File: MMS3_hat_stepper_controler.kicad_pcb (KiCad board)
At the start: 4 copper layers, 90 x 50 mm, 77 parts, among them J1 Chainbus in, J10 Conn_01x02, J11 Conn_01x02, J12 Conn_01x02, J2 Chainbus Out, J3 Conn_01x04_Pin, J4 AMASS XT60 Male, J5 AMASS XT60 Female, J6 Encoder connector, J7 Motor connector, J8 Conn_01x03_Pin, J9 Conn_01x02, U1 SN74CB3Q3384APW, U2 M24C64, U3 TMC5130A-TA, U4 AMS1117, U5 LM2596HVS-ADJRG

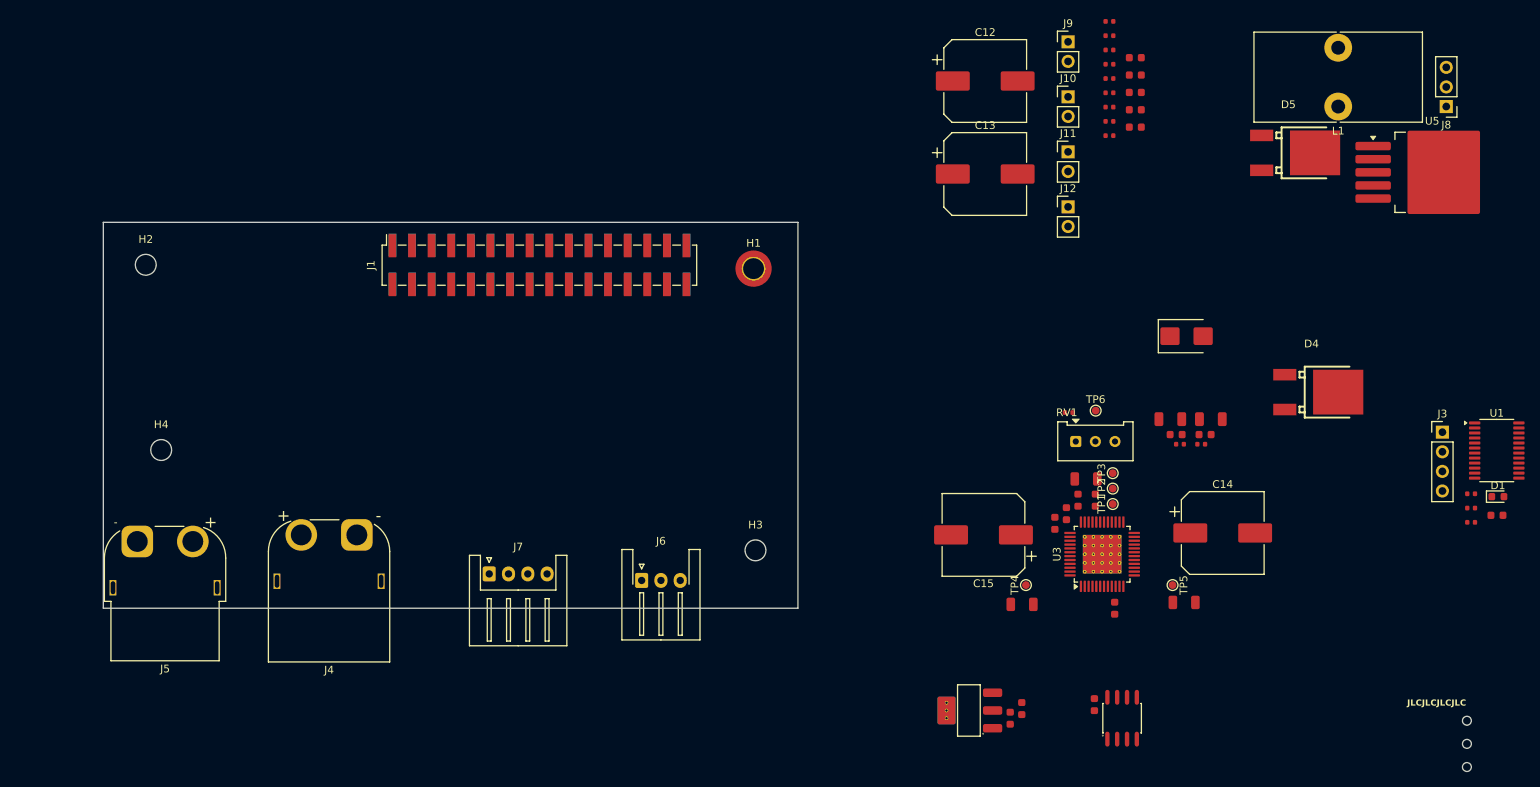
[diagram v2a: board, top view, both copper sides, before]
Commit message: added PCB from mechanical template
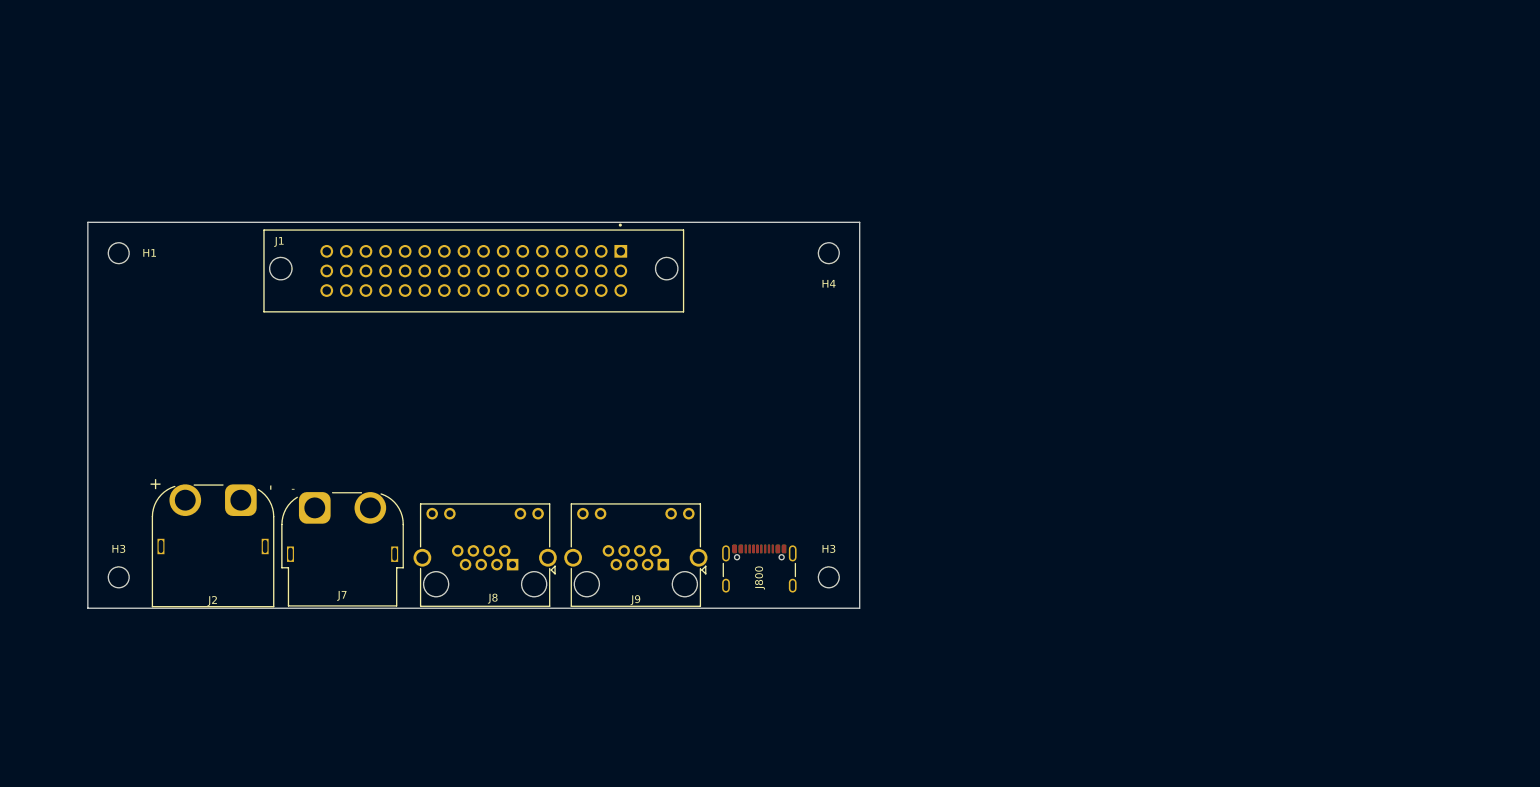
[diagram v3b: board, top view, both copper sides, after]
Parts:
- removed C1, C18, C19, C2, C21, C22, C3, C7, C8, C9: 100nF, PCM_JLCPCB:C_0603
- removed C10, C11: 4.7uF, PCM_JLCPCB:C_1206
- removed C12, C13, C14, C15: 100u, Capacitor_SMD:CP_Elec_10x12.5
- removed C16, C17: 10uF, PCM_JLCPCB:C_0603
- removed C20: 3.3nF, PCM_JLCPCB:C_0603
- removed C4: 4.7uF, PCM_JLCPCB:C_0603
- removed C5: 22nF, PCM_JLCPCB:C_0603
- removed C6: 470nF, PCM_JLCPCB:C_0603
- removed D1: LED, LED_SMD:LED_0603_1608Metric
- removed D3: SMBJ43CA, PCM_JLCPCB:D_SMB
- removed D4, D5: MBRD10100CTTR, SMC_MBRD10100CTTR:TO-252-3_L6.5-W5.8-P4.58-TL
- removed H2: M3 mount, MountingHole:MountingHole_2.7mm_M2.5_DIN965
- removed the H3 at (164.5, 130.5)
- removed H5, H6, H7: ~, PCM_JLCPCB:Hole_Tooling_JLCPCB
- removed J10, J11, J12: Conn_01x02, Connector_PinHeader_2.54mm:PinHeader_1x02_P2.54mm_Vertical
- removed J3: Conn_01x04_Pin, Connector_PinHeader_2.54mm:PinHeader_1x04_P2.54mm_Vertical
- removed J4: AMASS XT60 Male, XT60:AMASS_XT60PW-M_1x02_P7.20mm_Horizontal
- removed J5: AMASS XT60 Female, XT60:AMASS_XT60PW-F_1x02_P7.20mm_Horizontal
- removed J6: Encoder connector, Connector_JST:JST_XH_S3B-XH-A-1_1x03_P2.50mm_Horizontal
- removed L1: 100uH 5A, Inductor_THT:L_Toroid_Vertical_L21.6mm_W11.4mm_P7.62mm_Pulse_KM-3
- removed PN1: ~, PCM_JLCPCB:Part_Num_JLCPCB
- removed R1: 330Ω, PCM_JLCPCB:R_0402
- removed R10, R11, R17, R18, R8, R9: 33kΩ, PCM_JLCPCB:R_0402
- removed R12: 1kΩ, PCM_JLCPCB:R_0402
- removed R13: 18.7k, PCM_JLCPCB:R_0402
- removed R14: 16.5k, PCM_JLCPCB:R_0402
- removed R15: 9.53k, PCM_JLCPCB:R_0402
- removed R16: 5.11k, PCM_JLCPCB:R_0402
- removed R2, R3: 10kΩ, PCM_JLCPCB:R_0402
- removed R4: 0603/3R3, PCM_JLCPCB:R_1206
- removed R5: 100kΩ, PCM_JLCPCB:R_0402
- removed R6, R7: 1206, 0R15, 0.5W, PCM_JLCPCB:R_1206
- removed RV1: 100K TRIM, Potentiometer_THT:Potentiometer_Bourns_3386W_Horizontal
- removed TP1, TP2, TP3, TP4, TP5, TP6: TestPoint, TestPoint:TestPoint_Pad_D1.0mm
- removed U1: SN74CB3Q3384APW, Package_SO:TSSOP-24_4.4x7.8mm_P0.65mm
- removed U2: M24C64, PCM_JLCPCB:SOIC-8_L5.0-W4.0-P1.27-LS6.0-BL
- removed U3: TMC5130A-TA, Package_QFP:TQFP-48-1EP_7x7mm_P0.5mm_EP5x5mm_ThermalVias
- removed U4: AMS1117, PCM_JLCPCB:SOT-223-3_L6.5-W3.4-P2.30-LS7.0-BR
- removed U5: LM2596HVS-ADJRG, Package_TO_SOT_SMD:TO-263-5_TabPin3
- added G***: LOGO, QRcode:QR, B.Cu at (106.2, 117.5)
- added H3: M3 mount, MountingHole:MountingHole_2.7mm_M2.5, F.Cu at (174.0, 134.0)
- added H3: M3 mount, MountingHole:MountingHole_2.7mm_M2.5, F.Cu at (82.0, 134.0)
- added J800: USB_C_Receptacle_USB2.0_16P, Connector_USB:USB_C_Receptacle_GCT_USB4105-xx-A_16P_TopMnt_Horizontal, F.Cu at (165.0, 134.0)
- H1: footprint MountingHole:MountingHole_2.7mm_M2.5_DIN965_Pad_TopOnly -> MountingHole:MountingHole_2.7mm_M2.5
- H4: footprint MountingHole:MountingHole_2.7mm_M2.5_DIN965 -> MountingHole:MountingHole_2.7mm_M2.5
- J1: value Chainbus in -> 86093488324755V1LF; footprint Connector_PinSocket_2.54mm:PinSocket_2x16_P2.54mm_Vertical_SMD -> Library:AMPHENOL_86093488324755V1LF
- J2: value Chainbus Out -> AMASS XT60; footprint Connector_PinSocket_2.54mm:PinSocket_2x16_P2.54mm_Vertical_SMD -> XT60:AMASS_XT60PW-M_1x02_P7.20mm_Horizontal; moved to F.Cu
- J7: value Motor connector -> AMASS XT60; footprint Connector_JST:JST_XH_S4B-XH-A_1x04_P2.50mm_Horizontal -> XT60:AMASS_XT60PW-F_1x02_P7.20mm_Horizontal
- J8: value Conn_01x03_Pin -> RJ45_LED_Shielded; footprint Connector_PinHeader_2.54mm:PinHeader_1x03_P2.54mm_Vertical -> Connector_RJ:RJ45_Amphenol_RJHSE538X
- J9: value Conn_01x02 -> RJ45_LED_Shielded; footprint Connector_PinHeader_2.54mm:PinHeader_1x02_P2.54mm_Vertical -> Connector_RJ:RJ45_Amphenol_RJHSE538X
- moved J8 134.7 mm to (133.0, 132.3)
- moved H4 90.2 mm to (174.0, 92.0)
- moved J9 85.7 mm to (152.6, 132.3), turned to 180 degrees
- moved H1 82.3 mm to (82.0, 92.0)
- moved J2 49.3 mm to (97.8, 124.0), turned to 180 degrees
- moved J7 24.2 mm to (107.4, 125.0), turned to 180 degrees
- moved J1 8.53 mm to (128.0, 94.3), turned to 0 degrees
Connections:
- J2 pad 1: /Interboard_connector/SEL2 -> GNDPWR
- J2 pad 2: GND -> BRD_VIN
- J7 pad 1: /Stepper controller/OB1 -> GNDPWR
- J7 pad 2: /Stepper controller/OB2 -> BRD_VIN
- J8 pad 1: Net-(J8-Pin_1) -> /CAN auto terminator/CAN2.-
- J8 pad 2: Vin -> /CAN auto terminator/CAN2.+
- J8 pad 3: U_reg -> GND
- J9 pad 1: unconnected-(J9-Pin_1-Pad1) -> /CAN auto terminator/CAN2.-
- J9 pad 2: unconnected-(J9-Pin_2-Pad2) -> /CAN auto terminator/CAN2.+
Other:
- board size 90 x 50 mm -> 100 x 50 mm
- board text added: "+"
- board text added: "-"
- board text added: "2"
- board text added: "3V3"
- board text added: "5V0"
- board text added: "B G R C D 3"
- board text added: "CHAINBUS"
- board text added: "ChainBus"
- board text added: "DEVICE ESD SENSETIVE"
- board text added: "DIN41612"
- board text added: "Encloshure is supposed to have 2mm walls :)"
- board text added: "FW VER. MC1"
- board text added: "FW VER. MC2"
- board text added: "G"
- board text added: "GND"
- board text added: "IEC 60664-1 Material Group III (CTI < 400; typical FR-4 = IIIa): 1.25 mm"
- board text added: "IO R G"
- board text added: "MINI MODUCARD SYSTEM"
- board text added: "MMS"
- board text added: "Master link"
- board text added: "N/C"
- board text added: "QC"
- board text added: "SN"
- board text added: "This is prototype device It is not certified according to current EU laws. Do not sell or use outside of research purposes."
- board text added: "USB2.0"
- board text added: "VIN"
- board text added: "Ymin LKME5001J102MF"
- board text added: "arthorh.github.io/ChainBus"
- board text added: "connector powered by"
- board text added: "i"

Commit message: second component placement
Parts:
- removed the H3 at (174.0, 134.0)
- removed the H3 at (82.0, 134.0)
- removed J800: USB_C_Receptacle_USB2.0_16P, Connector_USB:USB_C_Receptacle_GCT_USB4105-xx-A_16P_TopMnt_Horizontal
- added C1: 100nF, PCM_JLCPCB:C_0603, F.Cu at (139.8, 108.5)
- added C10: 4.7uF, PCM_JLCPCB:C_1206, F.Cu at (145.2, 115.2)
- added C11: 4.7uF, PCM_JLCPCB:C_1206, F.Cu at (145.2, 120.0)
- added C12: 47u, Capacitor_SMD:CP_Elec_6.3x7.7, F.Cu at (140.2, 117.0)
- added C14: 47u, Capacitor_SMD:CP_Elec_6.3x7.7, F.Cu at (171.8, 110.5)
- added C15: 47u, Capacitor_SMD:CP_Elec_6.3x7.7, F.Cu at (171.6, 117.8)
- added C16: 10uF, PCM_JLCPCB:C_0603, F.Cu at (167.0, 92.3)
- added C17: 47u, Capacitor_SMD:CP_Elec_6.3x7.7, F.Cu at (83.0, 123.5)
- added C18: 10uF, PCM_JLCPCB:C_0603, F.Cu at (167.0, 95.3)
- added C19: 47u, Capacitor_SMD:CP_Elec_6.3x7.7, F.Cu at (83.0, 115.8)
- added C2: 100nF, PCM_JLCPCB:C_0603, F.Cu at (164.2, 104.0)
- added C20: 100nF, PCM_JLCPCB:C_0603, F.Cu at (91.5, 125.2)
- added C21: 100nF, PCM_JLCPCB:C_0603, F.Cu at (89.5, 126.2)
- added C22: 3.3nF, PCM_JLCPCB:C_0603, F.Cu at (106.5, 122.8)
- added C23: 100nF, PCM_JLCPCB:C_0603, F.Cu at (104.5, 102.2)
- added C24: 100nF, PCM_JLCPCB:C_0603, F.Cu at (104.5, 99.2)
- added C25: 47u, Capacitor_SMD:CP_Elec_6.3x7.7, F.Cu at (110.2, 105.0)
- added C26: 47u, Capacitor_SMD:CP_Elec_6.3x7.7, F.Cu at (117.8, 105.0)
- added C27: 47u, Capacitor_SMD:CP_Elec_6.3x7.7, F.Cu at (83.0, 108.2)
- added C28: 47u, Capacitor_SMD:CP_Elec_6.3x7.7, F.Cu at (125.2, 105.0)
- added C3: 100nF, PCM_JLCPCB:C_0603, F.Cu at (158.5, 120.8)
- added C4: 4.7uF, PCM_JLCPCB:C_0603, F.Cu at (157.0, 107.3)
- added C5: 22nF, PCM_JLCPCB:C_0603, F.Cu at (152.0, 109.1)
- added C6: 470nF, PCM_JLCPCB:C_0603, F.Cu at (154.0, 107.3)
- added C7: 100nF, PCM_JLCPCB:C_0603, F.Cu at (150.0, 111.8)
- added C8: 100nF, PCM_JLCPCB:C_0603, F.Cu at (147.0, 116.2)
- added C9: 100nF, PCM_JLCPCB:C_0603, F.Cu at (147.0, 119.2)
- added D1: LED, LED_SMD:LED_0603_1608Metric, F.Cu at (129.8, 137.0)
- added D2: MBRD10100CTTR, SMC_MBRD10100CTTR:TO-252-3_L6.5-W5.8-P4.58-TL, F.Cu at (125.7, 131.0)
- added D3: SMBJ43CA, PCM_JLCPCB:D_SMB, F.Cu at (144.8, 106.8)
- added D4: MBRD10100CTTR, SMC_MBRD10100CTTR:TO-252-3_L6.5-W5.8-P4.58-TL, F.Cu at (96.3, 106.7)
- added H2: M2.5 mount, MountingHole:MountingHole_2.7mm_M2.5, F.Cu at (174.0, 134.0)
- added H3: M2.5 mount, MountingHole:MountingHole_2.7mm_M2.5, F.Cu at (82.0, 92.0)
- added H5: M2.5 mount, MountingHole:MountingHole_2.7mm_M2.5, F.Cu at (103.0, 94.0)
- added H6: M2.5 mount, MountingHole:MountingHole_2.7mm_M2.5, F.Cu at (153.0, 94.0)
- added H7: ~, PCM_JLCPCB:Hole_Tooling_JLCPCB, F.Cu at (79.2, 136.8)
- added H8: ~, PCM_JLCPCB:Hole_Tooling_JLCPCB, F.Cu at (176.8, 89.2)
- added H9: ~, PCM_JLCPCB:Hole_Tooling_JLCPCB, F.Cu at (79.2, 89.2)
- added J10: Conn_01x02, Connector_PinHeader_2.54mm:PinHeader_1x02_P2.54mm_Horizontal, F.Cu at (116.5, 123.4)
- added J11: Conn_01x02, Connector_PinHeader_2.54mm:PinHeader_1x02_P2.54mm_Horizontal, F.Cu at (124.0, 123.4)
- added J12: Conn_01x02, Connector_PinHeader_2.54mm:PinHeader_1x02_P2.54mm_Horizontal, F.Cu at (131.5, 123.4)
- added J3: Conn_01x04_Pin, Connector_PinHeader_2.54mm:PinHeader_1x04_P2.54mm_Vertical, F.Cu at (151.2, 100.0)
- added J4: AMASS XT60 Male, XT60:AMASS_XT60PW-M_1x02_P7.20mm_Horizontal, F.Cu at (114.6, 129.6)
- added J5: AMASS XT60 Female, XT60:AMASS_XT60PW-F_1x02_P7.20mm_Horizontal, F.Cu at (90.4, 129.6)
- added J6: Encoder connector, Connector_JST:JST_XH_S3B-XH-A-1_1x03_P2.50mm_Horizontal, F.Cu at (151.2, 131.9)
- added L1: 100uH 4A, Inductor_SMD:L_Sunlord_SWRB1207S, F.Cu at (92.8, 95.5)
- added PN1: ~, PCM_JLCPCB:Part_Num_JLCPCB, F.Cu at (171.2, 88.8)
- added R1: 330Ω, PCM_JLCPCB:R_0402, F.Cu at (132.5, 136.8)
- added R10: 33kΩ, PCM_JLCPCB:R_0402, F.Cu at (89.0, 124.8)
- added R11: 33kΩ, PCM_JLCPCB:R_0402, F.Cu at (87.6, 126.0)
- added R12: 1kΩ, PCM_JLCPCB:R_0402, F.Cu at (106.2, 125.8)
- added R13: 18.7k, PCM_JLCPCB:R_0402, F.Cu at (114.0, 122.5)
- added R14: 16.5k, PCM_JLCPCB:R_0402, F.Cu at (121.5, 122.8)
- added R15: 9.53k, PCM_JLCPCB:R_0402, F.Cu at (129.0, 122.8)
- added R16: 5.11k, PCM_JLCPCB:R_0402, F.Cu at (136.8, 122.8)
- added R17: 33kΩ, PCM_JLCPCB:R_0402, F.Cu at (105.8, 102.2)
- added R18: 33kΩ, PCM_JLCPCB:R_0402, F.Cu at (105.8, 99.7)
- added R2: 10kΩ, PCM_JLCPCB:R_0402, F.Cu at (155.5, 97.5)
- added R3: 10kΩ, PCM_JLCPCB:R_0402, F.Cu at (156.5, 96.5)
- added R4: 0603/3R3, PCM_JLCPCB:R_1206, F.Cu at (156.0, 105.3)
- added R5: 100kΩ, PCM_JLCPCB:R_0402, F.Cu at (171.0, 123.8)
- added R6: 1206, 0R15, 0.5W, PCM_JLCPCB:R_1206, F.Cu at (150.2, 118.3)
- added R7: 1206, 0R15, 0.5W, PCM_JLCPCB:R_1206, F.Cu at (163.2, 118.1)
- added R8: 33kΩ, PCM_JLCPCB:R_0402, F.Cu at (148.0, 116.8)
- added R9: 33kΩ, PCM_JLCPCB:R_0402, F.Cu at (148.0, 118.8)
- added RV1: 100K TRIM, Potentiometer_THT:Potentiometer_Bourns_3296W_Vertical, F.Cu at (167.5, 125.2)
- added TP1: TestPoint, TestPoint:TestPoint_Pad_D1.0mm, F.Cu at (160.0, 104.8)
- added TP2: TestPoint, TestPoint:TestPoint_Pad_D1.0mm, F.Cu at (160.0, 106.8)
- added TP3: TestPoint, TestPoint:TestPoint_Pad_D1.0mm, F.Cu at (162.0, 106.8)
- added TP4: TestPoint, TestPoint:TestPoint_Pad_D1.0mm, F.Cu at (171.5, 125.8)
- added TP5: TestPoint, TestPoint:TestPoint_Pad_D1.0mm, F.Cu at (150.5, 114.6)
- added TP6: TestPoint, TestPoint:TestPoint_Pad_D1.0mm, F.Cu at (163.2, 114.6)
- added U1: SN74CB3Q3384APW, Package_SO:TSSOP-24_4.4x7.8mm_P0.65mm, F.Cu at (135.0, 106.5)
- added U2: M24C64, PCM_JLCPCB:SOIC-8_L5.0-W4.0-P1.27-LS6.0-BL, F.Cu at (166.0, 100.8)
- added U3: TMC5130A-TA, Package_QFP:TQFP-48-1EP_7x7mm_P0.5mm_EP5x5mm_ThermalVias, F.Cu at (156.8, 114.0)
- added U4: AMS1117, PCM_JLCPCB:SOT-223-3_L6.5-W3.4-P2.30-LS7.0-BR, F.Cu at (161.8, 93.8)
- added U5: LM2596HVS-ADJRG, Package_TO_SOT_SMD:TO-263-5_TabPin3, F.Cu at (99.2, 116.5)
- H1: value M3 mount -> M2.5 Mount; footprint MountingHole:MountingHole_2.7mm_M2.5 -> MountingHole:MountingHole_2.7mm_M2.5_DIN965_Pad_TopOnly
- H4: value M3 mount -> M2.5 mount
- J1: value 86093488324755V1LF -> Chainbus in; footprint Library:AMPHENOL_86093488324755V1LF -> Connector_PinHeader_2.54mm:PinHeader_2x16_P2.54mm_Vertical_SMD; moved to B.Cu
- J2: value AMASS XT60 -> Chainbus Out; footprint XT60:AMASS_XT60PW-M_1x02_P7.20mm_Horizontal -> Connector_PinSocket_2.54mm:PinSocket_2x16_P2.54mm_Vertical_SMD
- J7: value AMASS XT60 -> Motor connector; footprint XT60:AMASS_XT60PW-F_1x02_P7.20mm_Horizontal -> Connector_JST:JST_XH_S4B-XH-A_1x04_P2.50mm_Horizontal
- J8: value RJ45_LED_Shielded -> Conn_01x03_Pin; footprint Connector_RJ:RJ45_Amphenol_RJHSE538X -> Connector_PinHeader_2.54mm:PinHeader_1x03_P2.54mm_Vertical
- J9: value RJ45_LED_Shielded -> Conn_01x02; footprint Connector_RJ:RJ45_Amphenol_RJHSE538X -> Connector_PinHeader_2.54mm:PinHeader_1x02_P2.54mm_Horizontal
- moved J9 44.5 mm to (109.0, 123.4), turned to 90 degrees
- moved H1 42.0 mm to (82.0, 134.0)
- moved J2 41.5 mm to (128.0, 95.6), turned to 90 degrees
- moved J8 36.8 mm to (97.2, 124.2), turned to 90 degrees
- moved J7 30.6 mm to (137.5, 130.2), turned to 0 degrees
- moved J1 1.24 mm to (128.0, 95.5), turned to -90 degrees
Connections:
- J2 pad 1: GNDPWR -> GND
- J2 pad 2: BRD_VIN -> /Interboard_connector/SEL2
- J7 pad 1: GNDPWR -> /Stepper controller/OA1
- J7 pad 2: BRD_VIN -> /Stepper controller/OA2
- J8 pad 1: /CAN auto terminator/CAN2.- -> Net-(J8-Pin_1)
- J8 pad 2: /CAN auto terminator/CAN2.+ -> Vin
- J8 pad 3: GND -> U_reg
- J9 pad 1: /CAN auto terminator/CAN2.- -> unconnected-(J9-Pin_1-Pad1)
- J9 pad 2: /CAN auto terminator/CAN2.+ -> unconnected-(J9-Pin_2-Pad2)

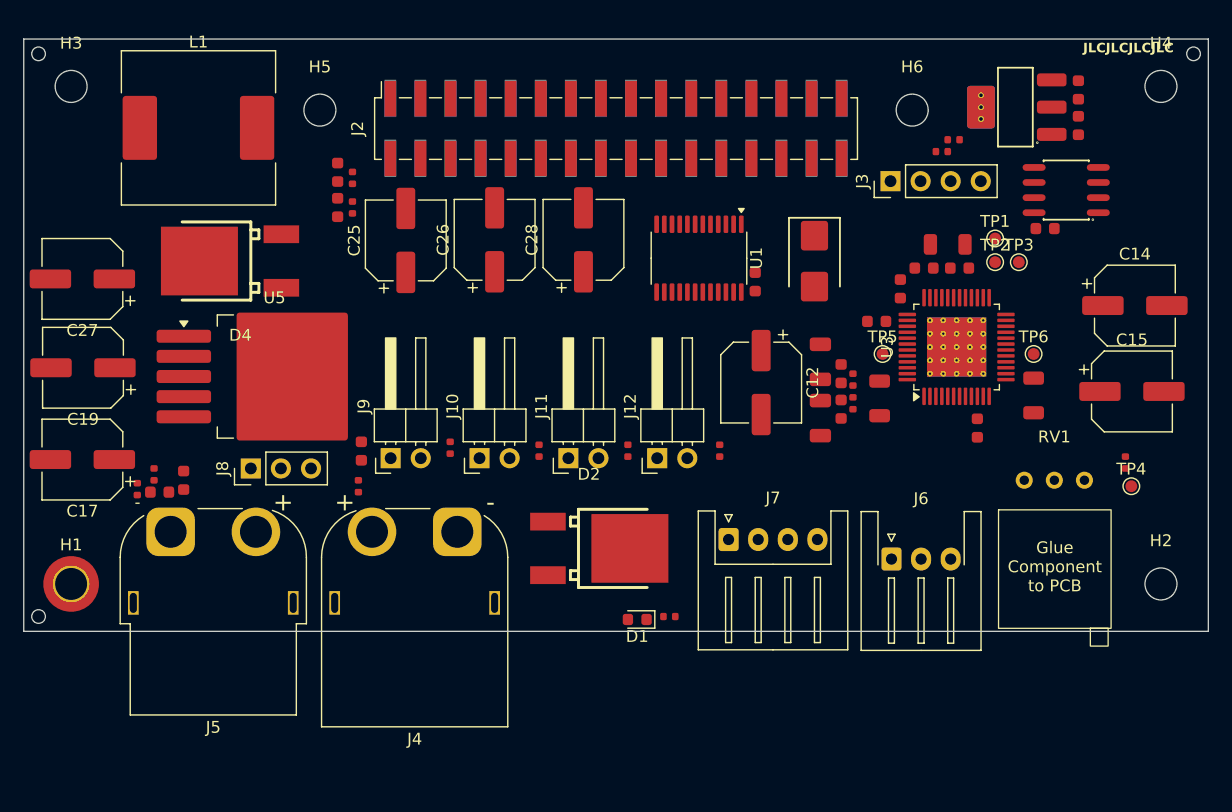
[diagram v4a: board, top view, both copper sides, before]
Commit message: Added design rules to PCB and updated dip switch
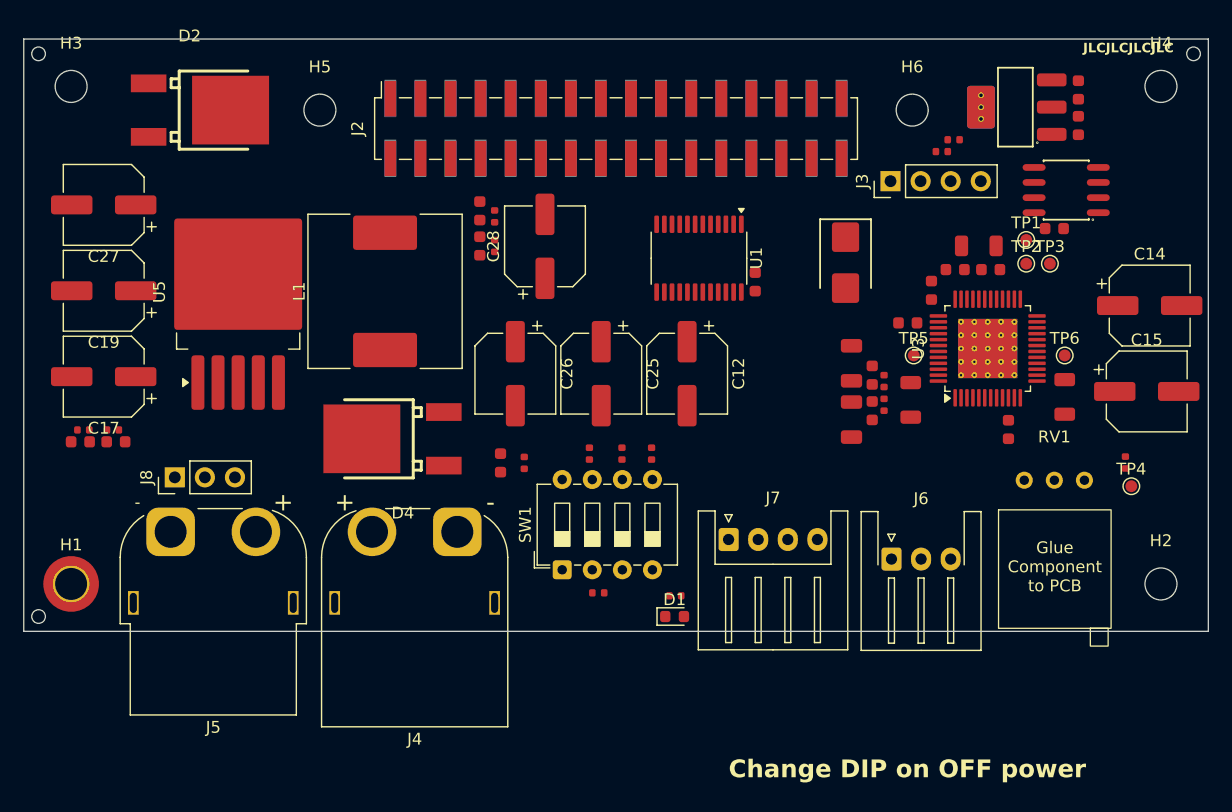
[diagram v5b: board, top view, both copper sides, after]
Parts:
- removed J10, J11, J12, J9: Conn_01x02, Connector_PinHeader_2.54mm:PinHeader_1x02_P2.54mm_Horizontal
- added SW1: SW_DIP_x04, Button_Switch_THT:SW_DIP_SPSTx04_Slide_6.7x11.72mm_W7.62mm_P2.54mm_LowProfile, F.Cu at (123.5, 132.8)
- moved D2 50.1 mm to (92.0, 94.0)
- moved R12 22.2 mm to (126.5, 134.8), turned to 180 degrees
- moved L1 20.9 mm to (108.5, 109.3), turned to 90 degrees
- moved D4 20.3 mm to (110.0, 121.8)
- moved C25 20.0 mm to (126.8, 116.2), turned to -90 degrees
- moved C23 12.4 mm to (116.5, 105.5)
- moved C24 12.4 mm to (116.5, 102.5)
- moved R17 12.4 mm to (117.8, 105.5)
- moved R18 12.4 mm to (117.8, 103.0)
- moved C22 11.8 mm to (118.2, 123.8)
- moved C26 11.4 mm to (119.5, 116.2), turned to -90 degrees
- moved C21 7.93 mm to (82.8, 122.0)
- moved U5 7.77 mm to (96.1, 109.3), turned to 90 degrees
- moved C17 7.23 mm to (84.8, 116.5)
- moved R11 6.76 mm to (83.0, 121.0), turned to 180 degrees
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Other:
- board text added: "Change DIP on OFF power"
